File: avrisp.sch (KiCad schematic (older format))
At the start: 25 parts, among them J3 USB_A, J4 CONN_02X05, U1 ATMEGA8-16PU, Y1 12MHz

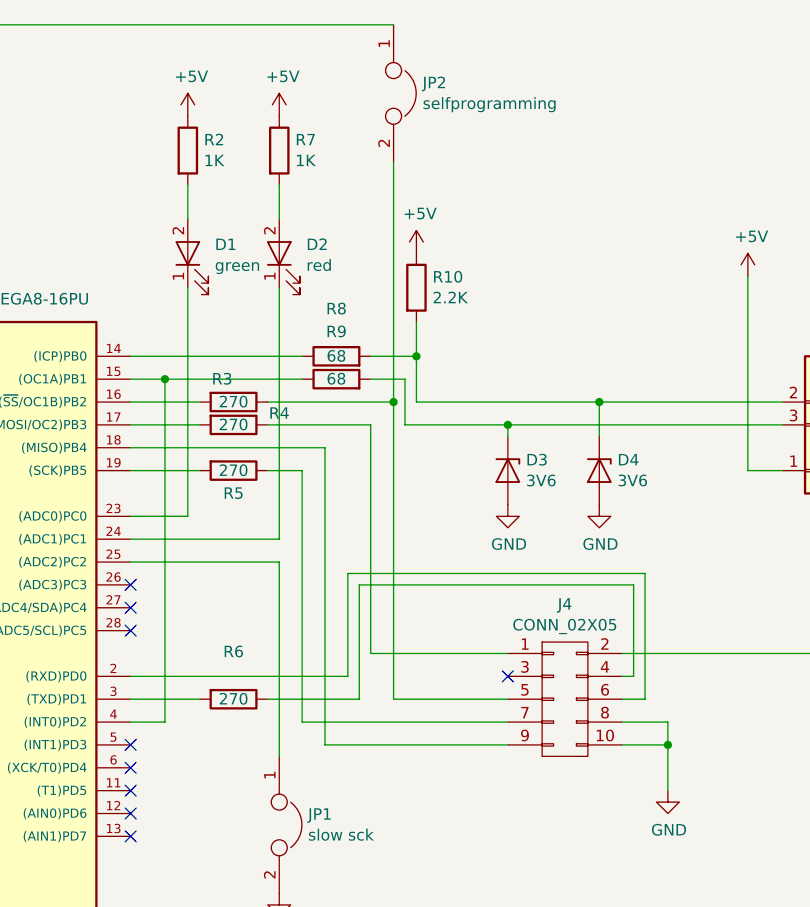
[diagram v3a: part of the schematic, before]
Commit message: Make one side version
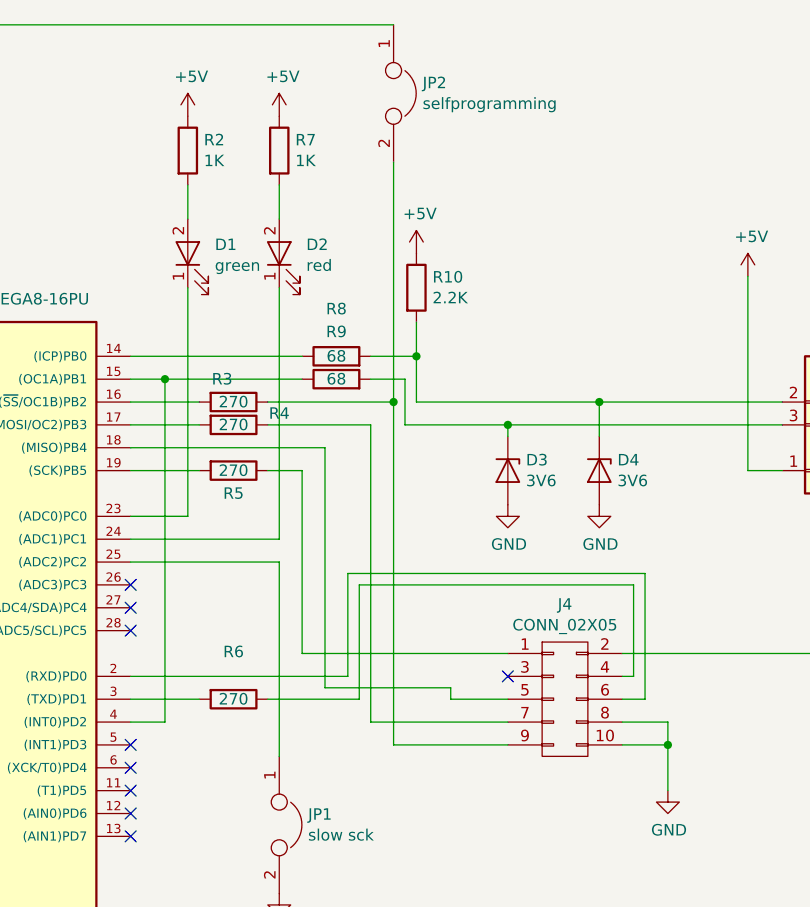
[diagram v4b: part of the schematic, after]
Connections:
- net at U1.18 ((MISO)PB4): now also J4.5 (P5); no longer J4.9 (P9)
- net at JP2.2, R3.1: now also J4.9 (P9); no longer J4.5 (P5)
- net at R4.1: now also J4.7 (P7); no longer J4.1 (P1)
- net at R5.1: now also J4.1 (P1); no longer J4.7 (P7)
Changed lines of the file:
@@
 	1    0    0    -1
 $EndComp
-Wire Wire Line
-	3750 3500 3600 3500
-Wire Wire Line
-	3600 3500 3600 4150
 $Comp
 L GND #PWR06
@@
 	1    0    0    -1
 $EndComp
-Wire Wire Line
-	4650 5700 4650 5800
-Wire Wire Line
-	3750 3100 3500 3100
-Wire Wire Line
-	3500 3100 3500 2900
-Wire Wire Line
-	3750 3300 3200 3300
-Wire Wire Line
-	3200 3300 3200 2600
 NoConn ~ 3750 3400
 $Comp
@@
 	1    0    0    -1
 $EndComp
-Wire Wire Line
-	3750 4000 2850 4000
-Wire Wire Line
-	2550 4000 2400 4000
-Wire Wire Line
-	2400 3800 2400 4300
-Wire Wire Line
-	2950 4300 2950 4000
-Connection ~ 2950 4000
-Wire Wire Line
-	3750 3800 2400 3800
-Connection ~ 2400 4000
 $Comp
 L GND #PWR011
@@
 	0    1    1    0
 $EndComp
-Wire Wire Line
-	5650 3200 6400 3200
-Wire Wire Line
-	5800 3200 5800 4700
-Wire Wire Line
-	5800 4700 5650 4700
-Wire Wire Line
-	5950 3300 5650 3300
-Wire Wire Line
-	5650 3400 5950 3400
-Wire Wire Line
-	5650 3600 5950 3600
-Wire Wire Line
-	5950 4600 5650 4600
 $Comp
 L LED D1
@@
 	0    -1   -1   0
 $EndComp
-Wire Wire Line
-	5900 2800 5900 3800
-Wire Wire Line
-	5900 3800 5650 3800
-Wire Wire Line
-	6300 3900 5650 3900
-Wire Wire Line
-	5900 2350 5900 2500
-Wire Wire Line
-	6300 2350 6300 2500
-Wire Wire Line
-	6300 2800 6300 3900
 $Comp
 L USB_A J3
@@
 	0    -1   -1   0
 $EndComp
-Wire Wire Line
-	5650 3100 6400 3100
-Wire Wire Line
-	6700 3100 6900 3100
-Wire Wire Line
-	6900 2950 6900 3300
-Wire Wire Line
-	6900 3300 8500 3300
 $Comp
 L R R9
@@
 	0    -1   -1   0
 $EndComp
-Connection ~ 5800 3200
-Wire Wire Line
-	6850 3400 8500 3400
-Wire Wire Line
-	6850 3400 6850 3200
-Wire Wire Line
-	6850 3200 6700 3200
 $Comp
 L +5V #PWR013
@@
 	1    0    0    -1
 $EndComp
-Wire Wire Line
-	7800 4800 8000 4800
-Wire Wire Line
-	8000 4700 8000 5000
-Wire Wire Line
-	7800 4700 8000 4700
-Connection ~ 8000 4800
 $Comp
 L +5V #PWR016
@@
 	1    0    0    -1
 $EndComp
-Wire Wire Line
-	7800 4400 10000 4400
-Wire Wire Line
-	7800 4500 7850 4500
-Wire Wire Line
-	7850 4500 7850 4100
-Wire Wire Line
-	7850 4100 6650 4100
-Wire Wire Line
-	6650 4100 6650 4600
-Wire Wire Line
-	6650 4600 6250 4600
-Wire Wire Line
-	7800 4600 7900 4600
-Wire Wire Line
-	7900 4600 7900 4050
-Wire Wire Line
-	7900 4050 6600 4050
-Wire Wire Line
-	6600 4050 6600 4500
-Wire Wire Line
-	6600 4500 5650 4500
-Wire Wire Line
-	7300 4400 6700 4400
-Wire Wire Line
-	6700 4400 6700 3400
-Wire Wire Line
-	6700 3400 6250 3400
 NoConn ~ 7300 4500
-Wire Wire Line
-	6250 3300 6800 3300
-Wire Wire Line
-	6800 4600 7300 4600
-Connection ~ 6800 3300
-Wire Wire Line
-	6800 1650 3700 1650
-Wire Wire Line
-	3700 1650 3700 3100
-Connection ~ 3700 3100
-Wire Wire Line
-	6400 3600 6250 3600
-Wire Wire Line
-	7300 4700 6400 4700
-Wire Wire Line
-	6400 4700 6400 3600
-Wire Wire Line
-	7300 4800 6500 4800
-Wire Wire Line
-	6500 4800 6500 3500
-Wire Wire Line
-	6500 3500 5650 3500
 NoConn ~ 5650 4800
 NoConn ~ 5650 4900
@@
 NoConn ~ 5650 4200
 NoConn ~ 5650 4300
-Wire Wire Line
-	5650 4000 6300 4000
 $Comp
 L R R10
@@
 	1    0    0    -1
 $EndComp
-Connection ~ 6900 3100
 $Comp
 L Jumper JP2
@@
 	0    1    1    0
 $EndComp
-Wire Wire Line
-	6800 2250 6800 4600
 $Comp
 L Jumper JP3
@@
 	1    0    0    -1
 $EndComp
-Wire Wire Line
-	6300 4000 6300 4850
-Wire Wire Line
-	9350 2750 9350 2850
-Wire Wire Line
-	8800 2750 9350 2750
-Wire Wire Line
-	8900 2750 8900 3000
-Wire Wire Line
-	8800 3000 8800 2750
-Connection ~ 8900 2750
-Wire Wire Line
-	8350 2750 8350 3600
-Wire Wire Line
-	8350 3600 8500 3600
-Wire Wire Line
-	7300 3450 7300 3400
-Connection ~ 7300 3400
-Wire Wire Line
-	7700 3450 7700 3300
-Connection ~ 7700 3300
 $Comp
 L GND #PWR019
@@
 	1    0    0    -1
 $EndComp
-Wire Wire Line
-	3250 3600 3250 3700
-Wire Wire Line
-	3250 3700 3600 3700
-Connection ~ 3600 3700
 $Comp
 L PWR_FLAG #FLG022
@@
 	1    0    0    -1
 $EndComp
-Wire Wire Line
-	2850 2750 2850 2850
-Wire Wire Line
-	2850 2850 3200 2850
-Connection ~ 3200 2850
 $Comp
 L +5V #PWR023
@@
 	1    0    0    -1
 $EndComp
-Wire Wire Line
-	4650 2800 4650 2350
 $Comp
 L D_Zener_SOT23 D3
@@
 	0    1    1    0
 $EndComp
+Wire Wire Line
+	3750 3500 3600 3500
+Wire Wire Line
+	3600 3500 3600 4150
+Wire Wire Line
+	4650 5700 4650 5800
+Wire Wire Line
+	3750 3100 3500 3100
+Wire Wire Line
+	3500 3100 3500 2900
+Wire Wire Line
+	3750 3300 3200 3300
+Wire Wire Line
+	3200 3300 3200 2600
+Wire Wire Line
+	3750 4000 2850 4000
+Wire Wire Line
+	2550 4000 2400 4000
+Wire Wire Line
+	2400 3800 2400 4300
+Wire Wire Line
+	2950 4300 2950 4000
+Connection ~ 2950 4000
+Wire Wire Line
+	3750 3800 2400 3800
+Connection ~ 2400 4000
+Wire Wire Line
+	5650 3200 6400 3200
+Wire Wire Line
+	5800 3200 5800 4700
+Wire Wire Line
+	5800 4700 5650 4700
+Wire Wire Line
+	5950 3300 5650 3300
+Wire Wire Line
+	5650 3400 5950 3400
+Wire Wire Line
+	5650 3600 5950 3600
+Wire Wire Line
+	5950 4600 5650 4600
+Wire Wire Line
+	5900 2800 5900 3800
+Wire Wire Line
+	5900 3800 5650 3800
+Wire Wire Line
+	6300 3900 5650 3900
+Wire Wire Line
+	5900 2350 5900 2500
+Wire Wire Line
+	6300 2350 6300 2500
+Wire Wire Line
+	6300 2800 6300 3900
+Wire Wire Line
+	5650 3100 6400 3100
+Wire Wire Line
+	6700 3100 6900 3100
+Wire Wire Line
+	6900 2950 6900 3300
+Wire Wire Line
+	6900 3300 8500 3300
+Connection ~ 5800 3200
+Wire Wire Line
+	6850 3400 8500 3400
+Wire Wire Line
+	6850 3400 6850 3200
+Wire Wire Line
+	6850 3200 6700 3200
+Wire Wire Line
+	7800 4800 8000 4800
+Wire Wire Line
+	8000 4700 8000 5000
+Wire Wire Line
+	7800 4700 8000 4700
+Connection ~ 8000 4800
+Wire Wire Line
+	7800 4400 10000 4400
+Wire Wire Line
+	7800 4500 7850 4500
+Wire Wire Line
+	7850 4500 7850 4100
+Wire Wire Line
+	7850 4100 6650 4100
+Wire Wire Line
+	6650 4100 6650 4600
+Wire Wire Line
+	6650 4600 6250 4600
+Wire Wire Line
+	7800 4600 7900 4600
+Wire Wire Line
+	7900 4600 7900 4050
+Wire Wire Line
+	7900 4050 6600 4050
+Wire Wire Line
+	6600 4050 6600 4500
+Wire Wire Line
+	6600 4500 5650 4500
+Wire Wire Line
+	6700 3400 6700 4700
+Wire Wire Line
+	6700 3400 6250 3400
+Wire Wire Line
+	6250 3300 6800 3300
+Connection ~ 6800 3300
+Wire Wire Line
+	6800 1650 3700 1650
+Wire Wire Line
+	3700 1650 3700 3100
+Connection ~ 3700 3100
+Wire Wire Line
+	6400 3600 6250 3600
+Wire Wire Line
+	6500 3500 5650 3500
+Wire Wire Line
+	5650 4000 6300 4000
+Connection ~ 6900 3100
+Wire Wire Line
+	6800 2250 6800 4800
+Wire Wire Line
+	6300 4000 6300 4850
+Wire Wire Line
+	9350 2750 9350 2850
+Wire Wire Line
+	8800 2750 9350 2750
+Wire Wire Line
+	8900 2750 8900 3000
+Wire Wire Line
+	8800 3000 8800 2750
+Connection ~ 8900 2750
+Wire Wire Line
+	8350 2750 8350 3600
+Wire Wire Line
+	8350 3600 8500 3600
+Wire Wire Line
+	7300 3450 7300 3400
+Connection ~ 7300 3400
+Wire Wire Line
+	7700 3450 7700 3300
+Connection ~ 7700 3300
+Wire Wire Line
+	3250 3600 3250 3700
+Wire Wire Line
+	3250 3700 3600 3700
+Connection ~ 3600 3700
+Wire Wire Line
+	2850 2750 2850 2850
+Wire Wire Line
+	2850 2850 3200 2850
+Connection ~ 3200 2850
+Wire Wire Line
+	4650 2800 4650 2350
+Wire Wire Line
+	6800 4800 7300 4800
+Wire Wire Line
+	6500 3500 6500 4550
+Wire Wire Line
+	6500 4550 7050 4550
+Wire Wire Line
+	7050 4550 7050 4600
+Wire Wire Line
+	7050 4600 7300 4600
+Wire Wire Line
+	6700 4700 7300 4700
+Wire Wire Line
+	6400 3600 6400 4400
+Wire Wire Line
+	6400 4400 7300 4400
 $EndSCHEMATC

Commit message: last changes
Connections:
- net data-: now reaches D4.3 (K), J3.2 (D-), R10.2, R8.2
- net data+: now reaches D3.3 (K), J3.3 (D+), R9.2
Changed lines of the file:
@@
 Wire Wire Line
 	6400 4400 7300 4400
+Text Label 8050 3300 0    60   ~ 0
+data-
+Text Label 8050 3400 0    60   ~ 0
+data+
 $EndSCHEMATC

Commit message: Make one sided PCB but with smd components
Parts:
- removed J3: USB_A, Connectors:USB_A, symbol USB_A
- removed J4: CONN_02X05, Connectors:IDC_Header_Straight_10pins, symbol CONN_02X05
- removed JP3: vtarget, Connectors_Molex:Molex_KK-6410-02_02x2.54mm_Straight, symbol Jumper
- removed R5: 270, Resistors_THT:R_Axial_DIN0207_L6.3mm_D2.5mm_P10.16mm_Horizontal, symbol R
- added J1: serial1, Connectors_Molex:Molex_KK-6410-02_02x2.54mm_Straight, symbol CONN_01X02
- added J2, J3: CONN_01X04, Connectors_Molex:Molex_KK-6410-04_04x2.54mm_Straight, symbol CONN_01X04
- added J4: power, Connectors_Molex:Molex_KK-6410-02_02x2.54mm_Straight, symbol CONN_01X02
- R1, R10, R2, R7, R8, R9: footprint Resistors_THT:R_Axial_DIN0207_L6.3mm_D2.5mm_P10.16mm_Horizontal -> Resistors_SMD:R_1206
- R3, R4: value 270 -> 0; footprint Resistors_THT:R_Axial_DIN0207_L6.3mm_D2.5mm_P10.16mm_Horizontal -> Resistors_SMD:R_1206
- R6: value 270 -> 1K; footprint Resistors_THT:R_Axial_DIN0207_L6.3mm_D2.5mm_P10.16mm_Horizontal -> Resistors_SMD:R_1206
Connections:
- net +5V: now also R3.1, R3.2, J3.1 (P1), J4.1 (P1)
- net GND: now also R4.1, R4.2, J3.4 (P4), J4.2 (P2)
- net data+: now also J3.3 (P3)
- net data-: now also J3.2 (P2)
- net reset: now reaches JP2.1, R1.2, U1.1 (PC6(~RESET~))
- net ss: now reaches U1.16 ((~SS~/OC1B)PB2)
- net ss: now also JP2.2, J2.1 (P1); no longer R3.2
- net mosi: now reaches U1.17 ((MOSI/OC2)PB3)
- net mosi: now also J2.2 (P2); no longer R4.2
- net miso: now reaches U1.18 ((MISO)PB4)
- net miso: now also J2.3 (P3)
- net sck: now reaches U1.19 ((SCK)PB5)
- net sck: now also J2.4 (P4)
- net rx: now reaches U1.2 ((RXD)PD0)
- net rx: now also J1.1 (P1)
- net tx: now reaches R6.2, U1.3 ((TXD)PD1)
- net at R6.1: now also J1.2 (P2)
- no-connect marks 10 -> 9
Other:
- moved on the sheet: JP1, R10
